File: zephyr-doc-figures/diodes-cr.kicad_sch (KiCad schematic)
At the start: 18 parts, among them SW1 SW_Push

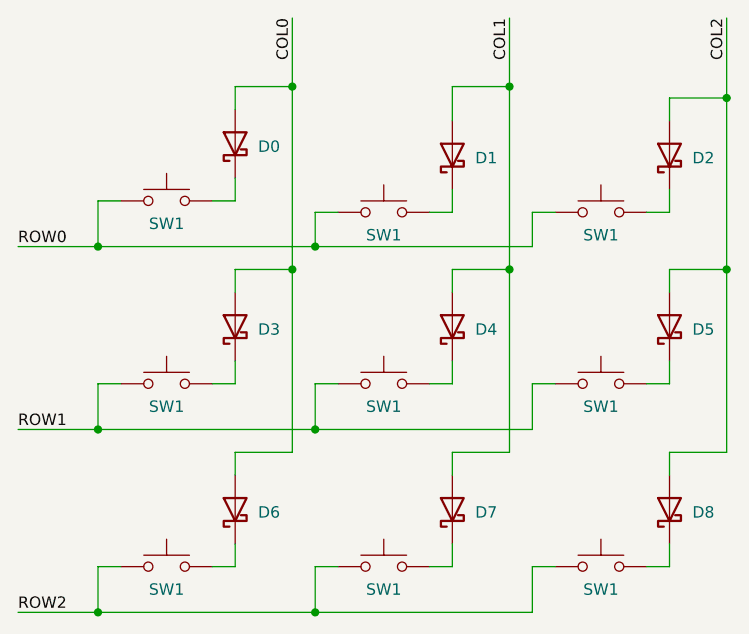
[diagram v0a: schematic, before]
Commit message: zephyr-doc-figures: update style and refdes
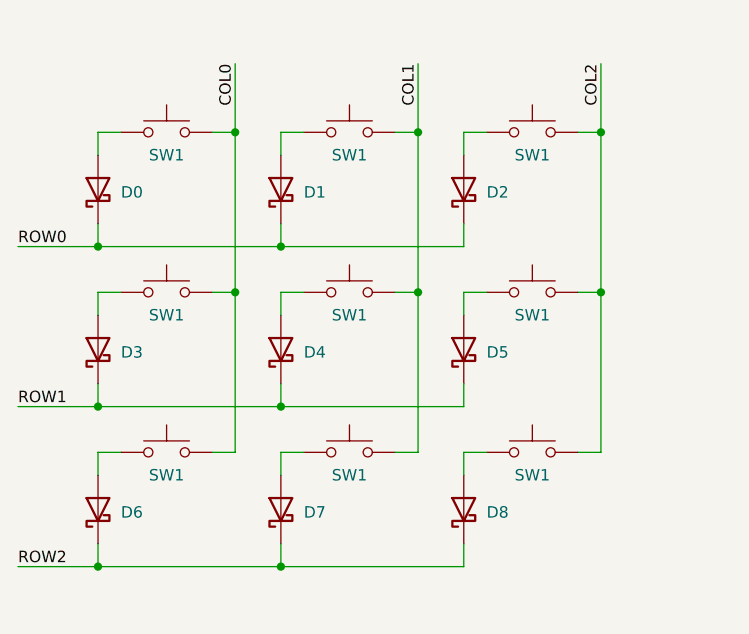
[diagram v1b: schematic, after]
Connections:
- net COL0: now also SW1.2, SW1.2, SW1.2; no longer D0.2 (A), D3.2 (A), D6.2 (A)
- net COL1: now also SW1.2, SW1.2, SW1.2; no longer D1.2 (A), D4.2 (A), D7.2 (A)
- net COL2: now also SW1.2, SW1.2, SW1.2; no longer D2.2 (A), D5.2 (A), D8.2 (A)
- net ROW0: now also D0.1 (K), D1.1 (K), D2.1 (K); no longer SW1.1, SW1.1, SW1.1
- net ROW1: now also D3.1 (K), D4.1 (K), D5.1 (K); no longer SW1.1, SW1.1, SW1.1
- net ROW2: now also D6.1 (K), D7.1 (K), D8.1 (K); no longer SW1.1, SW1.1, SW1.1
- new net: D4.2 (A), SW1.1
- new net: D1.2 (A), SW1.1
- new net: D7.2 (A), SW1.1
- new net: D8.2 (A), SW1.1
- new net: D3.2 (A), SW1.1
- new net: D0.2 (A), SW1.1
- new net: D5.2 (A), SW1.1
- new net: D6.2 (A), SW1.1
- new net: D2.2 (A), SW1.1
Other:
- moved on the sheet: D0, D1, D2, D3, D4, D5, D6, D7, D8, SW1
